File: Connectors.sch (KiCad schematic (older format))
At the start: 17 parts, among them J1 Conn_01x02, J10 Conn_01x08, J11 Conn_01x03, J12 Conn_01x02, J13 USB_B_Micro, J14 Conn_01x04, J15 Conn_01x04, J16 Conn_01x01, J17 Conn_01x04, J2 Conn_01x04, J3 Conn_01x04, J4 Conn_01x03, J5 Conn_01x03, J6 Conn_01x06, J7 Conn_01x06, J8 Conn_01x04, J9 Conn_01x08

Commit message: Lots of changes made
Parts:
- removed J14, J2: Conn_01x04, Connector_Wire:SolderWire-0.1sqmm_1x04_P3.6mm_D0.4mm_OD1mm, symbol Connector_Generic:Conn_01x04
- removed J6: Conn_01x06, Footprints:JST_SM06B-SRSS-TB(LF)(SN), symbol Connector_Generic:Conn_01x06
- removed J7: Conn_01x06, Connector_Wire:Connector_Wire_Solder_DJI, symbol Connector_Generic:Conn_01x06
- removed J8: Conn_01x04, Connector_PinHeader_2.54mm:PinHeader_1x04_P2.54mm_Vertical, symbol Connector_Generic:Conn_01x04
- added J11, J7: Conn_01x02, Connector_Wire:SolderWire-0.75sqmm_1x02_P4.8mm_D1.25mm_OD2.3mm, symbol Connector_Generic:Conn_01x02
- added J15, J9: Conn_01x04, Connector_Wire:SolderWire-0.1sqmm_1x04_P3.6mm_D0.4mm_OD1mm, symbol Connector_Generic:Conn_01x04
- added J17: Conn_01x01, Connector_Wire:SolderWire-0.1sqmm_1x01_D0.4mm_OD1mm, symbol Connector_Generic:Conn_01x01
- renumbered J5 to J1, J4 to J10, J11 to J12, J12 to J13, J3 to J14, J13 to J2, J9 to J3, J10 to J4, J17 to J5, J1 to J6, J15 to J8
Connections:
- net labels added: BUZ, CURR_SENSE, I2C2_SCL, I2C2_SDA, LED_STRIP, LIMIT1_INT, LIMIT2_INT, UART5_RX_CONN, UART5_TX_CONN, USART1_RX, USART1_TX, USART3_RX, USART3_TX, USART6_RX, USART6_TX, WORM1_H, WORM1_L, WORM2_H, WORM2_L
- net labels removed: +3V3, 4V5, BUZ-, CURR, I2C1_SCL, I2C1_SDA, LED, SWCLK, SWDIO, SWO, UART1_RX, UART1_TX, UART2_RX, UART2_TX, UART3_RX, UART3_TX, UART6_RX, UART6_TX
- wire segments 17 -> 11
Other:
- note removed: "DJI"
- note removed: "SWD"
- moved on the sheet: J10, J12, J13, J14, J6, J8

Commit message: Finished routing
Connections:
- net +5V: no longer J8.1 (Pin_1)
- new net +4V5: J8.1 (Pin_1)
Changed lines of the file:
@@
 	0    1    1    0
 $EndComp
-$Comp
-L power:+5V #PWR?
-U 1 1 60A8659D
-P 1650 6600
-AR Path="/60A8659D" Ref="#PWR?"  Part="1"
-AR Path="/60A7361B/60A8659D" Ref="#PWR080"  Part="1"
-F 0 "#PWR080" H 1650 6450 50  0001 C CNN
-F 1 "+5V" V 1650 6700 50  0000 L CNN
-F 2 "" H 1650 6600 50  0001 C CNN
-F 3 "" H 1650 6600 50  0001 C CNN
-	1    1650 6600
-	0    -1   -1   0
-$EndComp
 Text Notes 1500 6450 0    118  ~ 24
 UARTS
@@
 	1    0    0    -1
 $EndComp
+$Comp
+L power:+4V5 #PWR?
+U 1 1 6186F9D7
+P 1700 6600
+F 0 "#PWR?" H 1875 6675 50  0001 C CNN
+F 1 "+4V5" V 1685 6778 50  0000 L CNN
+F 2 "" H 1700 6600 50  0001 C CNN
+F 3 "" H 1700 6600 50  0001 C CNN
+	1    1700 6600
+	0    -1   -1   0
+$EndComp
 $EndSCHEMATC

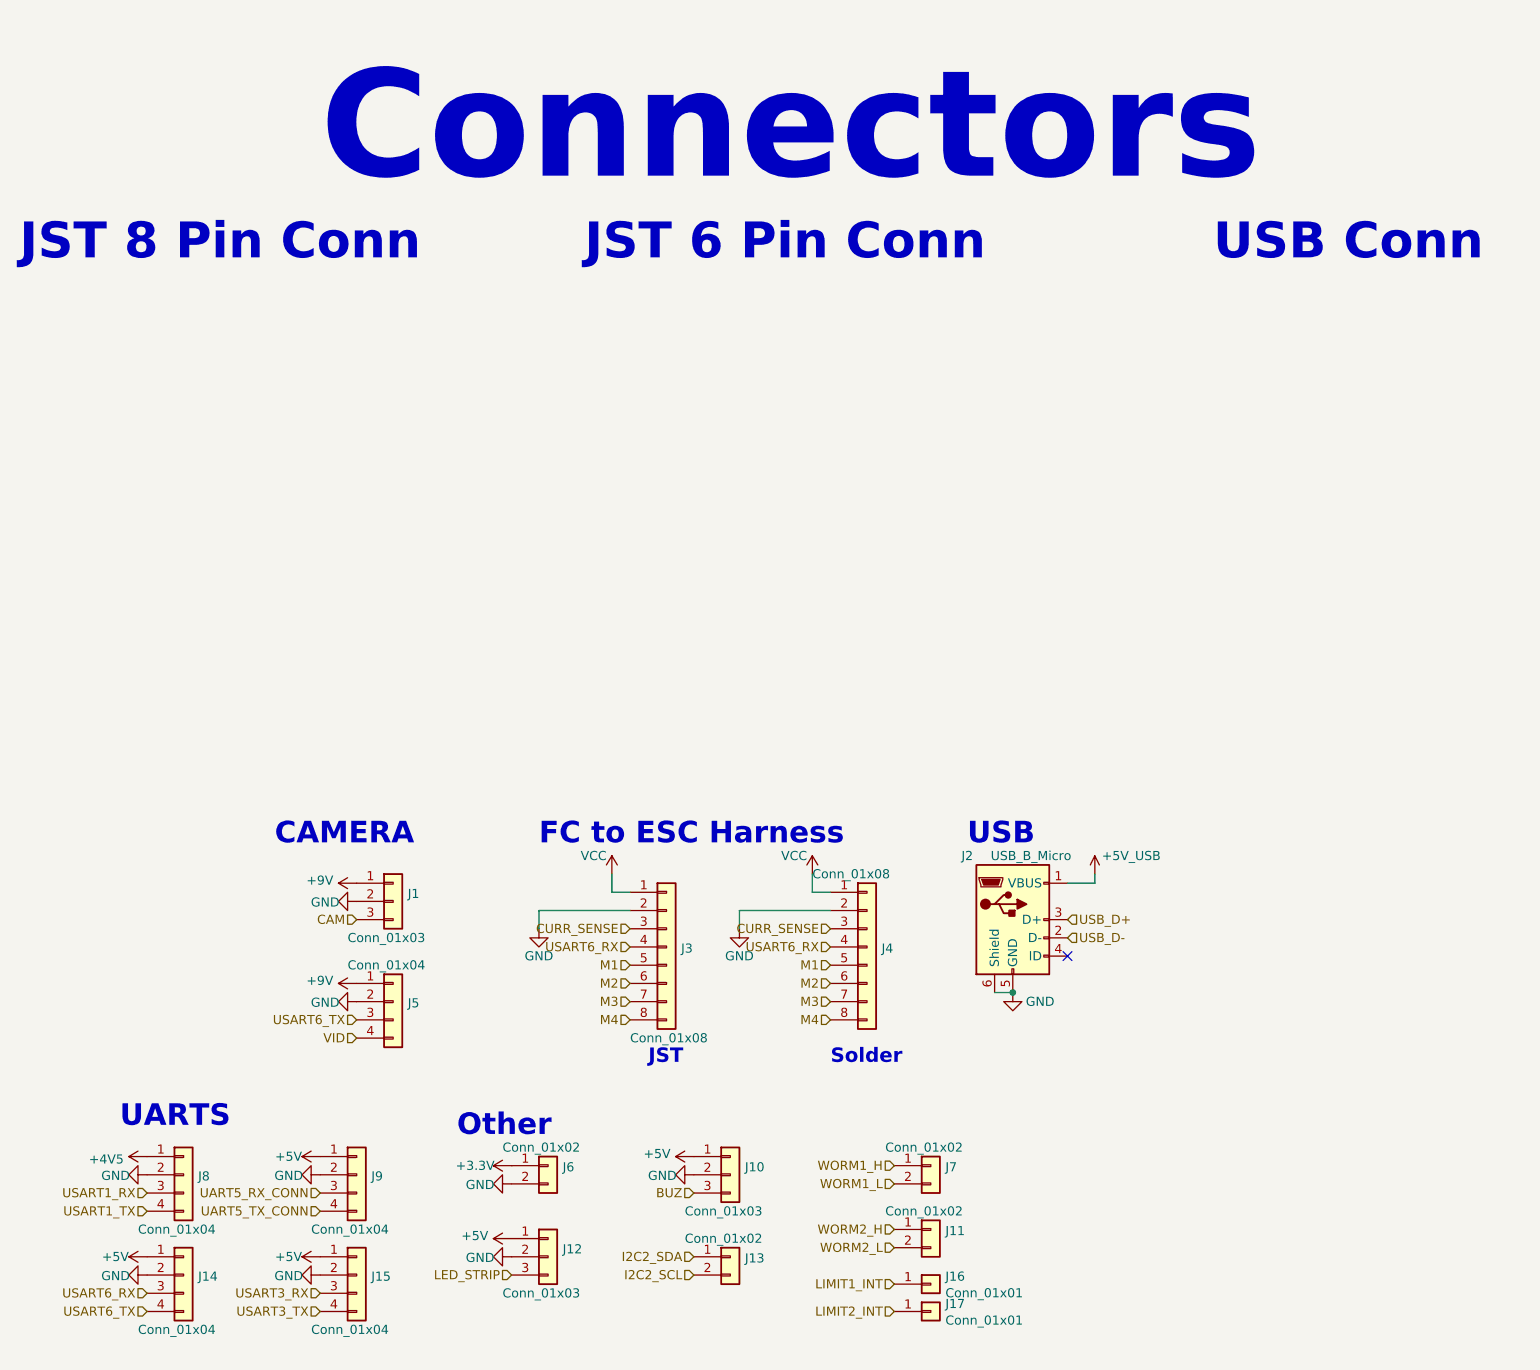
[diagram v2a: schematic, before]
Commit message: Increased board size and added silkscreen text
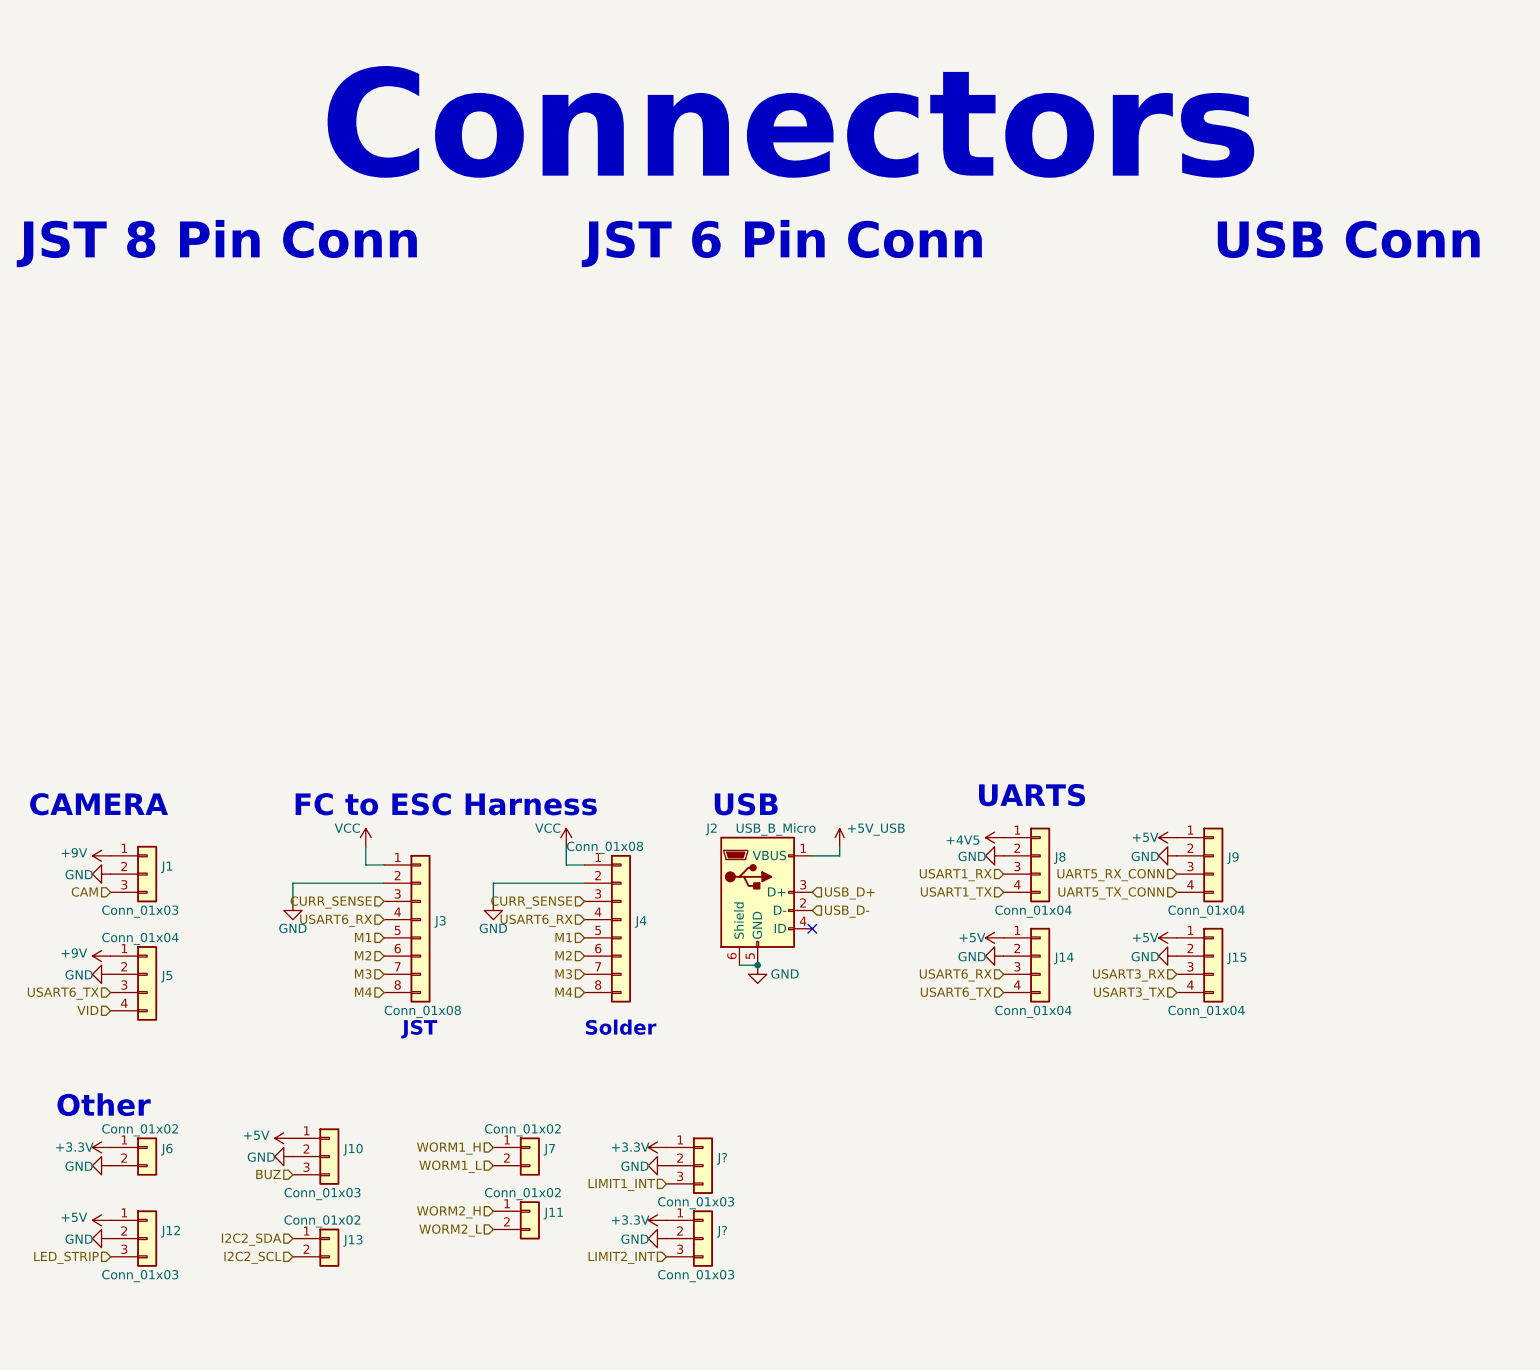
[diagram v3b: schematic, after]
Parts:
- removed J16, J17: Conn_01x01, Connector_Wire:SolderWire-0.1sqmm_1x01_D0.4mm_OD1mm, symbol Connector_Generic:Conn_01x01
- added J? (x2): Conn_01x03, Connector_Wire:SolderWire-0.1sqmm_1x03_P3.6mm_D0.4mm_OD1mm, symbol Connector_Generic:Conn_01x03
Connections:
- net +3V3: now also J?.1 (Pin_1), J?.1 (Pin_1)
- net GND: now also J?.2 (Pin_2), J?.2 (Pin_2)
- net LIMIT1_INT: now also J?.3 (Pin_3)
- net LIMIT2_INT: now also J?.3 (Pin_3)
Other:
- moved on the sheet: J1, J10, J11, J12, J13, J14, J15, J2, J3, J4, J5, J6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

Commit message: Changes made
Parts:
- J11: renamed from J7; footprint Connector_Wire:SolderWire-0.75sqmm_1x02_P4.8mm_D1.25mm_OD2.3mm -> Connector_Wire:SolderWire-0.25sqmm_1x02_P4.2mm_D0.65mm_OD1.7mm
- J14: renamed from J11; footprint Connector_Wire:SolderWire-0.75sqmm_1x02_P4.8mm_D1.25mm_OD2.3mm -> Connector_Wire:SolderWire-0.25sqmm_1x02_P4.2mm_D0.65mm_OD1.7mm
- gave numbers to parts that had none: 2
- renumbered J8 to J1, J6 to J10, J10 to J12, J12 to J15, J13 to J16, J9 to J2, J1 to J3, J2 to J4, J3 to J5, J4 to J6, J14 to J7, J15 to J8, J5 to J9
